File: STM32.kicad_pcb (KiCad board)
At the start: 2 copper layers, 38 x 38 mm, 32 parts, among them J1 USB_B_Micro, J2 Conn_01x04_Pin, J3 Conn_01x04_Pin, J4 Conn_01x04_Pin, SW1 SW_SPDT, U1 STM32F103C8T6, U2 AMS1117-3.3, Y1 16MHz

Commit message: add routing except for power supply
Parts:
- moved R1 4.25 mm to (107.7, 87.4), turned to 0 degrees
- moved C3 3.59 mm to (88.5, 70.2)
- moved FB1 2.65 mm to (85.2, 83.8)
- moved C10 2.64 mm to (83.3, 84.6)
- moved C9 2.45 mm to (83.3, 83.0)
- moved R4 2.10 mm to (86.0, 91.9)
- moved R5 2.09 mm to (88.0, 91.9)
- moved C2 1.58 mm to (103.5, 90.1)
- moved D1 1.44 mm to (107.2, 90.2)
- moved U2 0.97 mm to (98.7, 91.0)
- moved C7 0.43 mm to (93.9, 83.8)
- moved J1 0.40 mm to (106.3, 77.1)
- moved C5 0.15 mm to (88.5, 71.9)
- moved R3 0.10 mm to (99.8, 76.1)
- moved C8 0.10 mm to (85.1, 78.9)
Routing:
- net +3.3V: track 0.00 -> 36.9 mm
- net GND: track 0.00 -> 27.8 mm, vias 0 -> 20
- net /BOOT0: track 0.00 -> 21.7 mm
- net /SWDIO: track 0.00 -> 16.5 mm
- net /USART1_RX: track 0.00 -> 16.0 mm
- net /I2C2_SCL: track 0.00 -> 15.4 mm
- net /I2C2_SDA: track 0.00 -> 15.1 mm
- net /USART1_TX: track 0.00 -> 14.9 mm
- net /SWCLK: track 0.00 -> 12.0 mm
- net /USB_D-: track 0.00 -> 9.47 mm
- net /USB_D+: track 0.00 -> 9.39 mm
- net /HSE_IN: track 0.00 -> 9.02 mm
- net /NRST: track 0.00 -> 8.81 mm
- net /HSE_OUT: track 0.00 -> 7.30 mm
- net +3.3VA: track 0.00 -> 7.10 mm
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- added copper zone on B.Cu, net GND

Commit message: route all components
Added a new footprint for the spdt switch as DRC was throwing a warning
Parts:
- BOOT: renamed from SW1; footprint Button_Switch_SMD:SW_SPDT_PCM12 -> Boot_Switch:Boot_switch_custom
- moved C2 2.49 mm to (104.2, 87.7)
- moved VR 2.49 mm to (99.4, 88.6)
- moved C1 2.49 mm to (99.4, 82.8)
- moved R1 2.37 mm to (107.3, 85.0)
- moved PLED 2.26 mm to (107.2, 87.9)
- moved R4 0.69 mm to (86.0, 91.3)
- moved R5 0.69 mm to (88.0, 91.3)
- moved USB 0.12 mm to (106.2, 77.0)
- moved R3 0.08 mm to (99.8, 76.0)
- renumbered J4 to I2C, D1 to PLED, J2 to SWD, J3 to UART, J1 to USB, U2 to VR, Y1 to XO
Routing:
- net +3.3V: track 36.9 -> 170.5 mm, vias 0 -> 6
- net GND: track 27.8 -> 31.1 mm, vias 20 -> 22
- net /Power_Led_C: track 0.00 -> 2.25 mm
- added copper zone on F.Cu, net +3.3V
- added copper zone on F.Cu, net GND
- added copper zone on F.Cu, net VBUS

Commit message: fix routing, add bom, cpl and gbr files
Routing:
- net GND: track 31.1 -> 26.7 mm, vias 22 -> 20
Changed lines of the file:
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@@
 			(usegerberattributes yes)
 			(usegerberadvancedattributes yes)
-			(creategerberjobfile yes)
+			(creategerberjobfile no)
 			(dashed_line_dash_ratio 12)
 			(dashed_line_gap_ratio 3)
@@
 			(outputformat 1)
 			(mirror no)
-			(drillshape 1)
+			(drillshape 0)
 			(scaleselection 1)
-			(outputdirectory "")
+			(outputdirectory "Manufacturing/")
 		)
 	)
@@
 	)
 	(segment
-		(start 91.8718 62.865)
-		(end 91.8464 62.8396)
-		(width 0.5)
-		(layer "F.Cu")
-		(net "GND")
-	)
-	(segment
-		(start 79.121 62.865)
-		(end 79.0956 62.8396)
-		(width 0.5)
-		(layer "F.Cu")
-		(net "GND")
-	)
-	(segment
 		(start 89.0244 71.9328)
 		(end 89.0244 71.5544)
@@
 	)
 	(segment
-		(start 93.98 62.865)
-		(end 91.8718 62.865)
-		(width 0.5)
-		(layer "F.Cu")
-		(net "GND")
-	)
-	(segment
 		(start 88.7836 72.9128)
 		(end 89.0244 72.672)
@@
 	)
 	(segment
-		(start 81.28 62.865)
-		(end 79.121 62.865)
-		(width 0.5)
-		(layer "F.Cu")
-		(net "GND")
-	)
-	(segment
 		(start 82.4992 78.693971)
 		(end 83.009001 78.18417)
@@
 	)
 	(via
-		(at 91.8464 62.8396)
-		(size 0.7)
-		(drill 0.3)
-		(layers "F.Cu" "B.Cu")
-		(net "GND")
-	)
-	(via
 		(at 80.5434 75.4888)
 		(size 0.7)
@@
 		(net "GND")
 	)
-	(via
-		(at 79.0956 62.8396)
-		(size 0.7)
-		(drill 0.3)
-		(layers "F.Cu" "B.Cu")
-		(net "GND")
-	)

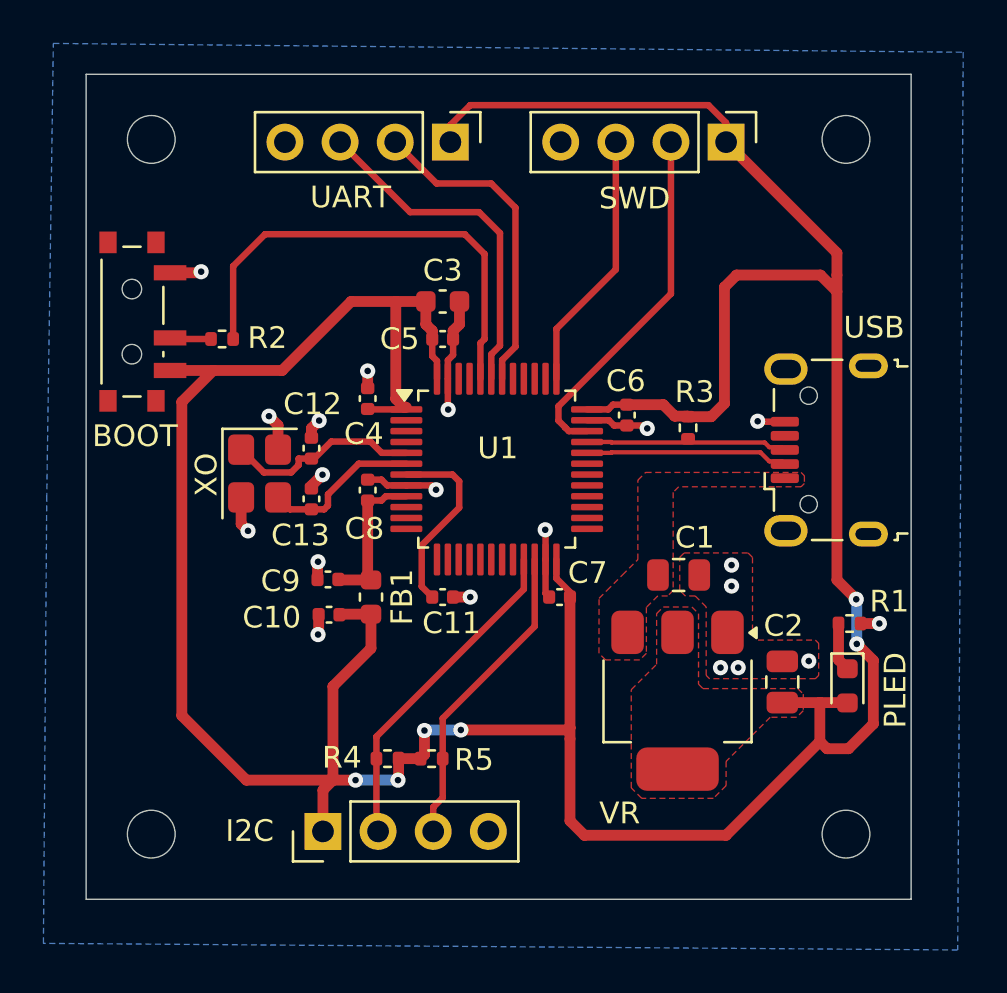
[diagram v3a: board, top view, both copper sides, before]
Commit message: Fix routing, regenerate manufacturing files and update readme
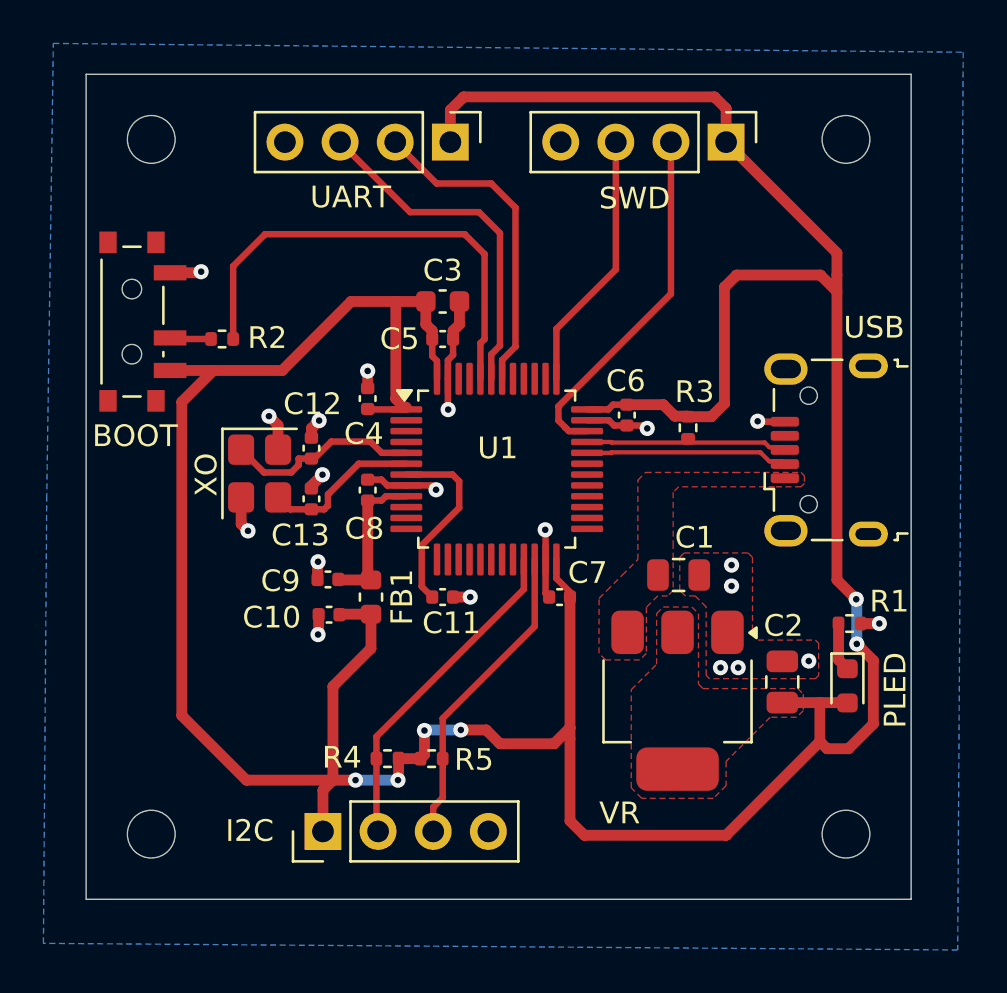
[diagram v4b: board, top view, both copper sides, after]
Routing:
- net +3.3V: track 170.5 -> 172.2 mm
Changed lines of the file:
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@@
+	)
+	(segment
+		(start 90.551 89.9414)
+		(end 89.3826 89.9414)
+		(width 0.5)
+		(layer "F.Cu")
+		(net "+3.3V")
 	)
 	(segment
@@
 	)
 	(segment
+		(start 89.5096 60.7822)
+		(end 88.9 61.3918)
+		(width 0.5)
+		(layer "F.Cu")
+		(net "+3.3V")
+	)
+	(segment
 		(start 108.3818 86.741)
 		(end 107.6198 85.979)
@@
 	)
 	(segment
+		(start 88.9 61.3918)
+		(end 88.9 62.865)
+		(width 0.5)
+		(layer "F.Cu")
+		(net "+3.3V")
+	)
+	(segment
 		(start 88.0644 72.7228)
 		(end 88.0644 71.9328)
@@
 	)
 	(segment
-		(start 94.3076 89.9414)
-		(end 89.3826 89.9414)
-		(width 0.5)
-		(layer "F.Cu")
-		(net "+3.3V")
-	)
-	(segment
 		(start 96.3904 74.958)
 		(end 97.028 74.958)
@@
 	)
 	(segment
+		(start 94.4092 89.8398)
+		(end 93.6726 90.5764)
+		(width 0.5)
+		(layer "F.Cu")
+		(net "+3.3V")
+	)
+	(segment
 		(start 88.0644 71.5544)
 		(end 87.7694 71.2594)
@@
 	)
 	(segment
+		(start 101.0666 60.7822)
+		(end 89.5096 60.7822)
+		(width 0.5)
+		(layer "F.Cu")
+		(net "+3.3V")
+	)
+	(segment
 		(start 88.0644 71.9328)
 		(end 88.0644 71.5544)
@@
 	)
 	(segment
-		(start 100.7872 61.1632)
-		(end 89.8144 61.1632)
-		(width 0.3)
-		(layer "F.Cu")
-		(net "+3.3V")
-	)
-	(segment
-		(start 94.4092 89.8398)
-		(end 94.3076 89.9414)
-		(width 0.5)
-		(layer "F.Cu")
-		(net "+3.3V")
-	)
-	(segment
 		(start 86.7711 75.0772)
 		(end 86.8711 75.0772)
@@
 	)
 	(segment
-		(start 101.6 62.865)
-		(end 101.6 61.976)
-		(width 0.3)
-		(layer "F.Cu")
-		(net "+3.3V")
-	)
-	(segment
 		(start 85.2424 84.6075)
 		(end 83.8173 84.6075)
@@
 	)
 	(segment
-		(start 88.9 62.0776)
-		(end 88.9 62.865)
-		(width 0.3)
-		(layer "F.Cu")
-		(net "+3.3V")
-	)
-	(segment
-		(start 89.8144 61.1632)
-		(end 88.9 62.0776)
-		(width 0.3)
-		(layer "F.Cu")
-		(net "+3.3V")
-	)
-	(segment
 		(start 105.918 90.4748)
 		(end 101.6 94.7928)
@@
 	)
 	(segment
+		(start 101.6 62.865)
+		(end 101.6 61.3156)
+		(width 0.5)
+		(layer "F.Cu")
+		(net "+3.3V")
+	)
+	(segment
 		(start 99.2358 75.4868)
 		(end 98.707 74.958)
@@
 	)
 	(segment
+		(start 91.186 90.5764)
+		(end 90.551 89.9414)
+		(width 0.5)
+		(layer "F.Cu")
+		(net "+3.3V")
+	)
+	(segment
 		(start 94.4092 89.8398)
 		(end 94.4092 83.82)
@@
 	)
 	(segment
+		(start 93.6726 90.5764)
+		(end 91.186 90.5764)
+		(width 0.5)
+		(layer "F.Cu")
+		(net "+3.3V")
+	)
+	(segment
 		(start 102.0826 68.9864)
 		(end 101.5238 69.5452)
@@
 	)
 	(segment
-		(start 101.6 61.976)
-		(end 100.7872 61.1632)
-		(width 0.3)
-		(layer "F.Cu")
-		(net "+3.3V")
+		(start 101.6 61.3156)
+		(end 101.0666 60.7822)
+		(width 0.5)
+		(layer "F.Cu")
+		(net "+3.3V")
